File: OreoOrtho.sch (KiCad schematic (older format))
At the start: 44 parts, among them SW1 MXSwitch, SW2 MXSwitch, SW3 MXSwitch, SW4 MXSwitch, SW5 MXSwitch, SW6 MXSwitch, SW7 MXSwitch, SW8 MXSwitch, U1 ATmega32U4-AU, Y1 16MHz

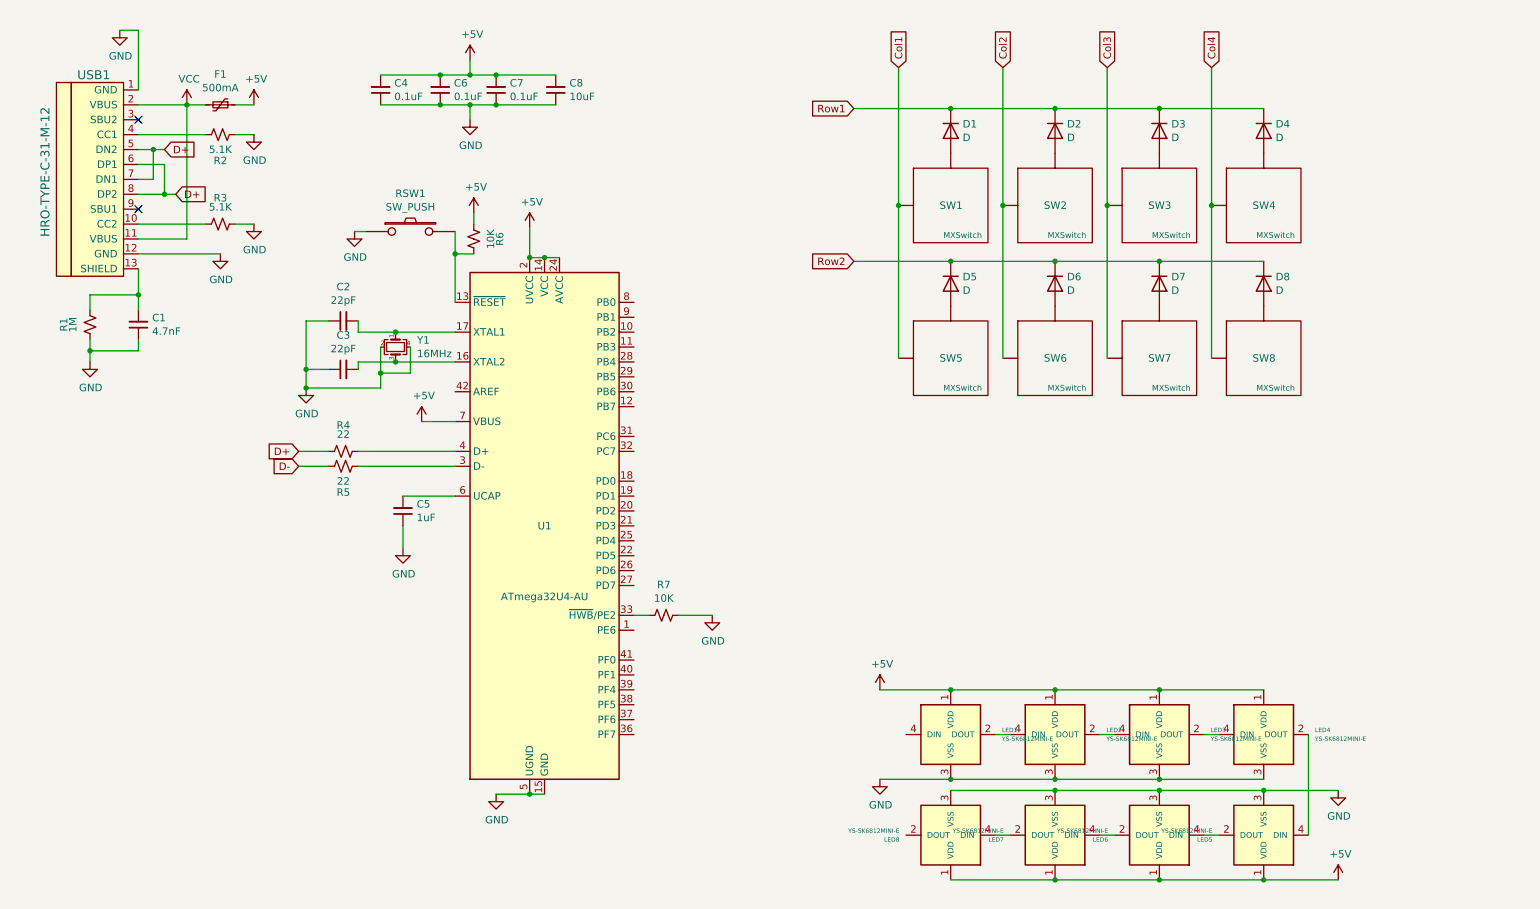
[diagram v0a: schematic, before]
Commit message: new mcu, fuse, etc
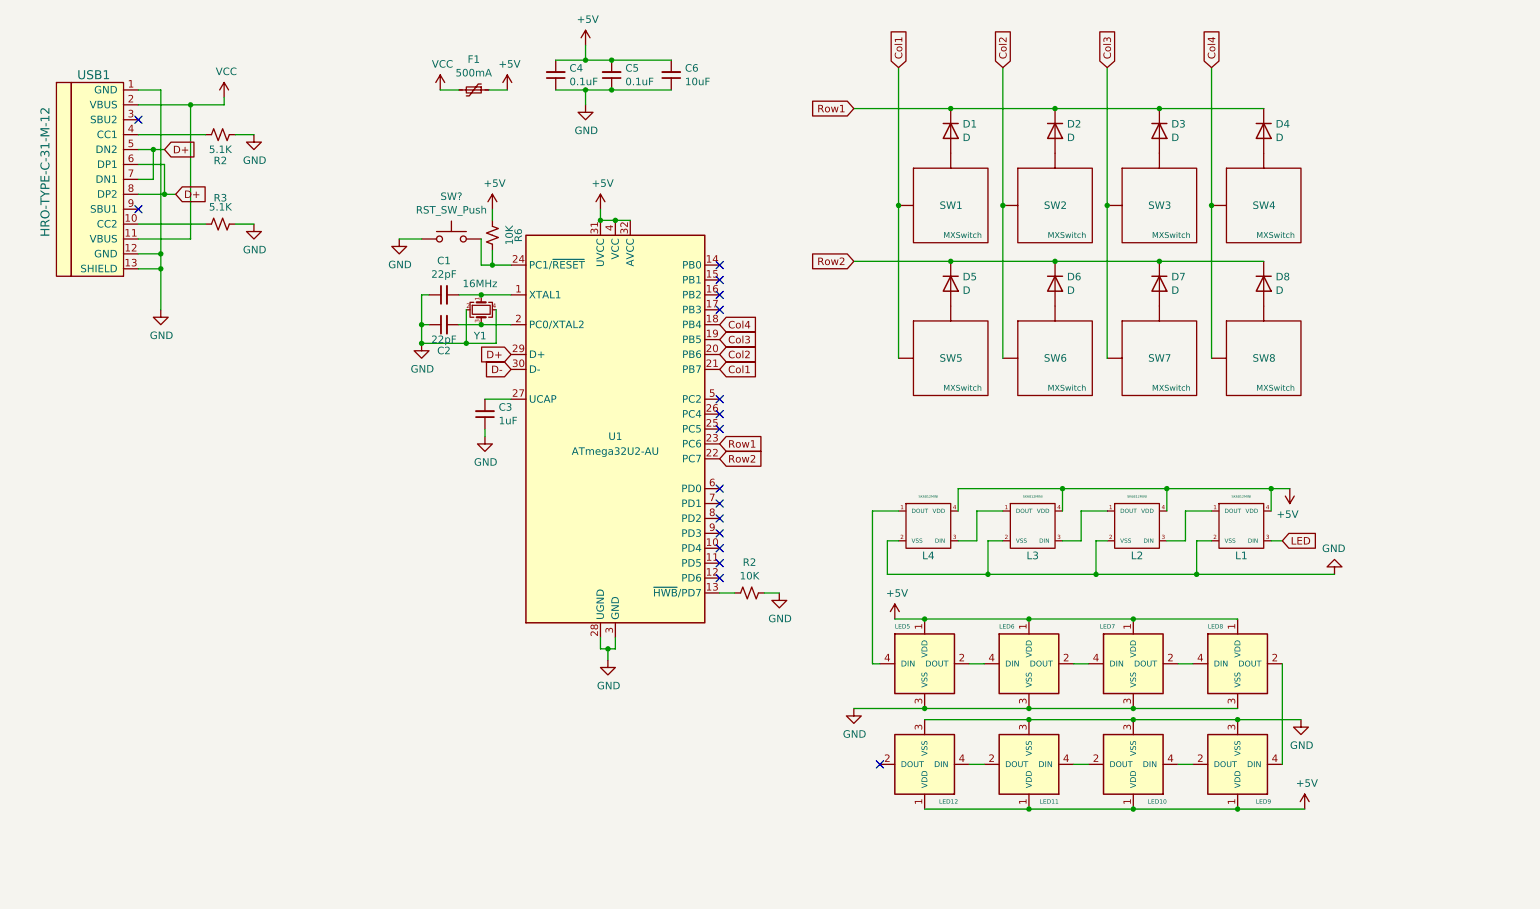
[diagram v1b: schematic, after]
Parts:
- removed C1: 4.7nF, symbol Device:C_Small
- removed C4: 0.1uF, symbol Device:C_Small
- removed R1: 1M, symbol Device:R_Small_US
- removed R4, R5: 22, symbol Device:R_Small_US
- removed RSW1: SW_PUSH, symbol kbd:SW_PUSH
- removed U1: ATmega32U4-AU, Package_QFP:TQFP-44_10x10mm_P0.8mm, symbol MCU_Microchip_ATmega:ATmega32U4-AU
- added L1, L2, L3, L4: SK6812MINI, LED_SMD:LED_SK6812MINI_PLCC4_3.5x3.5mm_P1.75mm, symbol kbd:SK6812MINI
- added SW?: RST_SW_Push, symbol Switch:SW_Push
- added U1: ATmega32U2-AU, Package_QFP:TQFP-32_7x7mm_P0.8mm, symbol MCU_Microchip_ATmega:ATmega32U2-AU
- C1: renamed from C3; footprint (none) -> Capacitor_SMD:C_0805_2012Metric
- C2: footprint (none) -> Capacitor_SMD:C_0805_2012Metric
- C3: renamed from C5; footprint (none) -> Capacitor_SMD:C_0805_2012Metric
- C4: renamed from C6; footprint (none) -> Capacitor_SMD:C_0805_2012Metric
- C5: renamed from C7; footprint (none) -> Capacitor_SMD:C_0805_2012Metric
- C6: renamed from C8; footprint (none) -> Capacitor_SMD:C_0805_2012Metric
- D1, D2, D3, D4, D5, D6, D7, D8: footprint (none) -> Diode_SMD:D_SOD-123
- F1: footprint (none) -> Fuse:Fuse_1206_3216Metric
- LED10: renamed from LED4; footprint (none) -> kbd:SK6812-MINI-E
- LED11: renamed from LED3; footprint (none) -> kbd:SK6812-MINI-E
- LED12: renamed from LED8; footprint (none) -> kbd:SK6812-MINI-E
- LED5, LED6: footprint (none) -> kbd:SK6812-MINI-E
- LED7: renamed from LED2; footprint (none) -> kbd:SK6812-MINI-E
- LED8: renamed from LED7; footprint (none) -> kbd:SK6812-MINI-E
- LED9: renamed from LED1; footprint (none) -> kbd:SK6812-MINI-E
- R2: renamed from R7; footprint (none) -> Resistor_SMD:R_0805_2012Metric
- R2, R3, R6: footprint (none) -> Resistor_SMD:R_0805_2012Metric
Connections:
- net +5V: now also L1.4 (VDD), L2.4 (VDD), L3.4 (VDD), L4.4 (VDD), U1.31 (UVCC), U1.32 (AVCC), U1.4 (VCC)
- net Col1: now also U1.21 (PB7)
- net Col2: now also U1.20 (PB6)
- net Col3: now also U1.19 (PB5)
- net Col4: now also U1.18 (PB4)
- net D+: now also U1.29 (D+)
- net D-: now also U1.30 (D-)
- net GND: now also USB1.13 (SHIELD), L1.2 (VSS), L2.2 (VSS), L3.2 (VSS), L4.2 (VSS), SW?.1, U1.28 (UGND), U1.3 (GND)
- net Row1: now also U1.23 (PC6)
- net Row2: now also U1.22 (PC7)
- net at R6.1: now also SW?.2, U1.24 (PC1/~RESET)
- net at C1.2: now also Y1.1, U1.1 (XTAL1); no longer Y1.3
- net at C2.2: now also Y1.3, U1.2 (PC0/XTAL2); no longer Y1.1
- net at R2.2: now also U1.13 (~HWB~/PD7)
- net at C3.2: now also U1.27 (UCAP)
- net at LED7.2 (DOUT): now also LED8.4 (DIN); no longer LED11.4 (DIN)
- net at LED7.4 (DIN): now also LED6.2 (DOUT); no longer LED9.2 (DOUT)
- net at LED11.2 (DOUT): now also LED12.4 (DIN); no longer LED10.4 (DIN)
- net at LED10.2 (DOUT): now also LED11.4 (DIN); no longer LED5.4 (DIN)
- net at LED8.2 (DOUT): now also LED9.4 (DIN); no longer LED12.4 (DIN)
- new net: LED10.4 (DIN), LED9.2 (DOUT)
- new net: L4.1 (DOUT), LED5.4 (DIN)
- new net: L1.1 (DOUT), L2.3 (DIN)
- new net: L2.1 (DOUT), L3.3 (DIN)
- new net: L3.1 (DOUT), L4.3 (DIN)
- new net LED: L1.3 (DIN)
- no-connect marks 2 -> 17
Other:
- moved on the sheet: C1, C2, C3, C4, C5, C6, F1, LED10, LED11, LED12, LED5, LED6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

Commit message: changed mcu, usb
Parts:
- removed D7, D8: D, Diode_SMD:D_SOD-123, symbol Device:D
- removed L1, L2, L3, L4: SK6812MINI, LED_SMD:LED_SK6812MINI_PLCC4_3.5x3.5mm_P1.75mm, symbol kbd:SK6812MINI
- removed LED8, LED9: YS-SK6812MINI-E, kbd:SK6812-MINI-E, symbol kbd:YS-SK6812MINI-E
- removed SW2, SW3, SW4, SW5, SW6, SW7, SW8: MXSwitch, symbol acheronSymbols:MXSwitch
- added R4, R5: 22, Resistor_SMD:R_0805_2012Metric, symbol Device:R_Small_US
- added SW2, SW3, SW4, SW5, SW6: MXSwitch, kbd:CherryMX_1u, symbol kbd:SW_PUSH
- added U2: PRTR5V0U2X, Package_TO_SOT_SMD:SOT-143, symbol Power_Protection:PRTR5V0U2X
- C1, C2, C3, C4, C5, C6: footprint Capacitor_SMD:C_0805_2012Metric -> Capacitor_SMD:C_0603_1608Metric
- D1, D2, D3, D4, D5, D6: footprint Diode_SMD:D_SOD-123 -> kbd:D3_SMD_v2
- LED1: renamed from LED5; footprint kbd:SK6812-MINI-E -> kbd:YS-SK6812MINI-E
- LED2: renamed from LED6; footprint kbd:SK6812-MINI-E -> kbd:YS-SK6812MINI-E
- LED3: renamed from LED7; footprint kbd:SK6812-MINI-E -> kbd:YS-SK6812MINI-E
- LED4: renamed from LED10; footprint kbd:SK6812-MINI-E -> kbd:YS-SK6812MINI-E
- LED5: renamed from LED11; footprint kbd:SK6812-MINI-E -> kbd:YS-SK6812MINI-E
- LED6: renamed from LED12; footprint kbd:SK6812-MINI-E -> kbd:YS-SK6812MINI-E
- RST_SW1: renamed from SW?; value RST_SW_Push -> SW_Push; footprint (none) -> random-keyboard-parts:SKQG-1155865
- SW1: footprint (none) -> kbd:CherryMX_1u; symbol acheronSymbols:MXSwitch -> kbd:SW_PUSH
- USB1: footprint (none) -> Type-C:HRO-TYPE-C-31-M-12-Assembly; symbol keebio:HRO-TYPE-C-31-M-12 -> Type-C:HRO-TYPE-C-31-M-12
- Y1: footprint (none) -> Crystal:Crystal_SMD_3225-4Pin_3.2x2.5mm_HandSoldering
- renumbered R6 to R1, R2 to R3, R3 to R6
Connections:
- net Col3 is gone; now on net Col2: U1.19 (PB5)
- net Col4 is gone; now on net LED: U1.18 (PB4)
- net Col1: now also U1.20 (PB6), SW2.1, SW5.1; no longer SW1.1 (Col), U1.21 (PB7)
- net Col2: now also SW3.1, SW6.1; no longer U1.20 (PB6)
- net D+: now also R4.2; no longer USB1.5 (DN2), USB1.6 (DP1), USB1.7 (DN1), USB1.8 (DP2)
- net D-: now also R5.1
- net GND: now also R3.2, R6.2, U2.1 (GND); no longer R3.1, R6.1
- net LED: now also LED1.4 (DIN)
- net Row1: now also D5.1 (K), D6.1 (K), U1.26 (PC4); no longer D1.1 (K), D2.1 (K), D3.1 (K), U1.23 (PC6)
- net VCC: now also U2.4 (VCC)
- net at D2.2 (A): now also SW2.2
- net at D3.2 (A): now also SW3.2
- net at D4.2 (A): now also SW4.2
- net at USB1.10 (CC2): now also R6.1; no longer R6.2
- net at USB1.4 (CC1): now also R3.1; no longer R3.2
- net at D5.2 (A): now also SW5.2
- net at D6.2 (A): now also SW6.2
- net at LED3.2 (DOUT): now also LED4.4 (DIN)
- net Row0: now reaches U1.5 (PC2)
- net Row0: now also D1.1 (K), D2.1 (K), D3.1 (K)
- removed net Row2: D5.1 (K), D6.1 (K), U1.22 (PC7)
- new net: R5.2, U2.2 (I/O1), USB1.5 (DN2), USB1.7 (DN1)
- new net: R4.1, U2.3 (I/O2), USB1.6 (DP1), USB1.8 (DP2)
- new net Col0: SW1.1, SW4.1, U1.21 (PB7)
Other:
- moved on the sheet: C1, C2, C3, C4, C5, C6, D1, F1, LED1, LED2, LED3, LED4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

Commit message: route ver1
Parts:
- removed D3, D6: D, kbd:D3_SMD_v2, symbol Device:D
- removed LED5, LED6: YS-SK6812MINI-E, kbd:YS-SK6812MINI-E, symbol kbd:YS-SK6812MINI-E
- removed SW3, SW6: MXSwitch, kbd:CherryMX_1u, symbol kbd:SW_PUSH
- added H1: MountingHole, kbd:HOLE, symbol Mechanical:MountingHole
- renumbered D4 to D3, D5 to D4, SW4 to SW3, SW5 to SW4
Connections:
- net Row0: now also U1.23 (PC6); no longer U1.5 (PC2)
- net Row1: now also U1.22 (PC7); no longer U1.26 (PC4)
- net Col2: no longer names the net of U1.19 (PB5)
- no-connect marks 17 -> 18
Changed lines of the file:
@@
 Wire Wire Line
 	1925 4250 1925 4450
-Text GLabel 5825 2425 2    50   Input ~ 0
+Text GLabel 5825 2725 2    50   Input ~ 0
 Row1
 Text GLabel 5825 2025 2    50   Input ~ 0
 Col1
-Text GLabel 5825 1925 2    50   Input ~ 0
-Col2
 $Comp
 L MCU_Microchip_ATmega:ATmega32U2-AU U1
@@
 Wire Wire Line
 	8025 1375 8025 1950
-Connection ~ 8725 1375
-Wire Wire Line
-	8725 1375 8725 1950
-Connection ~ 9425 1375
-Wire Wire Line
-	9425 1375 9425 1950
-Connection ~ 9325 1675
-Connection ~ 9325 2250
-$Comp
-L kbd:SW_PUSH SW4
+$Comp
+L kbd:SW_PUSH SW3
 U 1 1 60136BE3
 P 8325 1950
-F 0 "SW4" H 8250 1950 50  0000 L CNN
+F 0 "SW3" H 8250 1950 50  0000 L CNN
 F 1 "MXSwitch" H 8175 1875 39  0000 L CNN
 F 2 "kbd:CherryMX_1u" H 8325 1950 50  0001 C CNN
@@
 	8475 2250 8625 2250
 $Comp
-L kbd:SW_PUSH SW5
+L kbd:SW_PUSH SW4
 U 1 1 60136BF5
 P 9025 1950
-F 0 "SW5" H 8950 1950 50  0000 L CNN
+F 0 "SW4" H 8950 1950 50  0000 L CNN
 F 1 "MXSwitch" H 8875 1875 39  0000 L CNN
 F 2 "kbd:CherryMX_1u" H 9025 1950 50  0001 C CNN
@@
 $EndComp
 $Comp
-L Device:D D5
+L Device:D D4
 U 1 1 60136BFB
 P 9325 2100
-F 0 "D5" H 9275 2225 50  0000 L CNN
+F 0 "D4" H 9275 2225 50  0000 L CNN
 F 1 "D" H 9300 2000 50  0000 L CNN
 F 2 "kbd:D3_SMD_v2" H 9325 2100 50  0001 C CNN
@@
 $EndComp
 Connection ~ 8625 2250
-$Comp
-L kbd:SW_PUSH SW6
-U 1 1 60136C05
-P 9725 1950
-F 0 "SW6" H 9650 1950 50  0000 L CNN
-F 1 "MXSwitch" H 9575 1875 39  0000 L CNN
-F 2 "kbd:CherryMX_1u" H 9725 1950 50  0001 C CNN
-F 3 "" H 9725 1950 50  0001 C CNN
-	1    9725 1950
-	1    0    0    -1
-$EndComp
-$Comp
-L Device:D D6
-U 1 1 60136C0B
-P 10025 2100
-F 0 "D6" H 9975 2225 50  0000 L CNN
-F 1 "D" H 10000 2000 50  0000 L CNN
-F 2 "kbd:D3_SMD_v2" H 10025 2100 50  0001 C CNN
-F 3 "~" H 10025 2100 50  0001 C CNN
-	1    10025 2100
-	0    -1   -1   0
-$EndComp
-Wire Wire Line
-	9325 2250 10025 2250
-Wire Wire Line
-	9325 1675 10025 1675
-Wire Wire Line
-	9425 1375 9425 1150
-$Comp
-L Device:D D3
-U 1 1 6012380C
-P 10025 1525
-F 0 "D3" H 9975 1650 50  0000 L CNN
-F 1 "D" H 10000 1425 50  0000 L CNN
-F 2 "kbd:D3_SMD_v2" H 10025 1525 50  0001 C CNN
-F 3 "~" H 10025 1525 50  0001 C CNN
-	1    10025 1525
-	0    -1   -1   0
-$EndComp
-$Comp
-L kbd:SW_PUSH SW3
-U 1 1 60123806
-P 9725 1375
-F 0 "SW3" H 9650 1375 50  0000 L CNN
-F 1 "MXSwitch" H 9575 1300 39  0000 L CNN
-F 2 "kbd:CherryMX_1u" H 9725 1375 50  0001 C CNN
-F 3 "" H 9725 1375 50  0001 C CNN
-	1    9725 1375
-	1    0    0    -1
-$EndComp
-Text GLabel 9425 1150 1    50   Input ~ 0
-Col2
 Connection ~ 8625 1675
 Wire Wire Line
 	8625 1675 9325 1675
-Wire Wire Line
-	8725 1375 8725 1150
 $Comp
 L Device:D D2
@@
 	0    -1   -1   0
 $EndComp
-$Comp
-L kbd:SW_PUSH SW2
-U 1 1 6011665D
-P 9025 1375
-F 0 "SW2" H 8950 1375 50  0000 L CNN
-F 1 "MXSwitch" H 8875 1300 39  0000 L CNN
-F 2 "kbd:CherryMX_1u" H 9025 1375 50  0001 C CNN
-F 3 "" H 9025 1375 50  0001 C CNN
-	1    9025 1375
-	1    0    0    -1
-$EndComp
 Wire Wire Line
 	8025 1375 8025 1150
@@
 Wire Wire Line
 	7575 4000 7625 4000
-NoConn ~ 7625 4675
+NoConn ~ 9025 4675
 Text GLabel 7575 4000 0    50   Input ~ 0
 LED
@@
 $EndComp
 Wire Wire Line
-	8625 4975 9325 4975
-Connection ~ 8625 4975
-Connection ~ 8625 4375
-Wire Wire Line
-	7925 4375 8625 4375
-Wire Wire Line
-	7925 4975 8625 4975
-Wire Wire Line
 	8225 4000 8325 4000
 $Comp
@@
 	9725 4000 9725 4675
 Wire Wire Line
-	8325 4675 8225 4675
-Wire Wire Line
-	9025 4675 8925 4675
-Wire Wire Line
 	9725 4675 9625 4675
-$Comp
-L kbd:YS-SK6812MINI-E LED6
-U 1 1 5F923BDB
-P 7925 4675
-F 0 "LED6" H 7700 4925 29  0000 L CNN
-F 1 "YS-SK6812MINI-E" H 8269 4646 29  0001 L CNN
-F 2 "kbd:YS-SK6812MINI-E" H 8025 4425 50  0001 C CNN
-F 3 "" H 8025 4425 50  0001 C CNN
-	1    7925 4675
-	-1   0    0    1
-$EndComp
 $Comp
 L kbd:YS-SK6812MINI-E LED2
@@
 	8925 4000 9025 4000
 $Comp
-L kbd:YS-SK6812MINI-E LED5
-U 1 1 5F8F9075
-P 8625 4675
-F 0 "LED5" H 8425 4925 29  0000 L CNN
-F 1 "YS-SK6812MINI-E" H 8969 4646 29  0001 L CNN
-F 2 "kbd:YS-SK6812MINI-E" H 8725 4425 50  0001 C CNN
-F 3 "" H 8725 4425 50  0001 C CNN
-	1    8625 4675
-	-1   0    0    1
-$EndComp
-$Comp
 L kbd:YS-SK6812MINI-E LED3
 U 1 1 5F8F886B
@@
 Text GLabel 5825 2125 2    50   Input ~ 0
 Col0
-Text GLabel 5825 2325 2    50   Input ~ 0
+Text GLabel 5825 2625 2    50   Input ~ 0
 Row0
 NoConn ~ 5825 1725
 Text GLabel 5825 1825 2    50   Input ~ 0
 LED
-Wire Wire Line
-	8625 4375 9325 4375
-Connection ~ 9325 4375
 $Comp
 L kbd:YS-SK6812MINI-E LED4
@@
 	-1   0    0    1
 $EndComp
-Connection ~ 9325 4975
 Wire Wire Line
 	1325 1500 1700 1500
@@
 Connection ~ 1775 3850
 NoConn ~ 5825 2525
-NoConn ~ 5825 2625
-NoConn ~ 5825 2725
+NoConn ~ 5825 2425
+NoConn ~ 5825 2325
 Wire Wire Line
 	9325 4975 9775 4975
@@
 	9325 4375 9900 4375
 $Comp
-L Device:D D4
+L Device:D D3
 U 1 1 60136BE9
 P 8625 2100
-F 0 "D4" H 8575 2225 50  0000 L CNN
+F 0 "D3" H 8575 2225 50  0000 L CNN
 F 1 "D" H 8600 2000 50  0000 L CNN
 F 2 "kbd:D3_SMD_v2" H 8625 2100 50  0001 C CNN
@@
 	0    -1   -1   0
 $EndComp
+Wire Wire Line
+	8725 1375 8725 1150
+Wire Wire Line
+	8725 1375 8725 1950
+Connection ~ 8725 1375
+$Comp
+L kbd:SW_PUSH SW2
+U 1 1 6011665D
+P 9025 1375
+F 0 "SW2" H 8950 1375 50  0000 L CNN
+F 1 "MXSwitch" H 8875 1300 39  0000 L CNN
+F 2 "kbd:CherryMX_1u" H 9025 1375 50  0001 C CNN
+F 3 "" H 9025 1375 50  0001 C CNN
+	1    9025 1375
+	1    0    0    -1
+$EndComp
+NoConn ~ 5825 1925
+$Comp
+L Mechanical:MountingHole H1
+U 1 1 5F929254
+P 1025 5700
+F 0 "H1" H 1125 5746 50  0000 L CNN
+F 1 "MountingHole" H 1125 5655 50  0000 L CNN
+F 2 "kbd:HOLE" H 1025 5700 50  0001 C CNN
+F 3 "~" H 1025 5700 50  0001 C CNN
+	1    1025 5700
+	1    0    0    -1
+$EndComp
 $EndSCHEMATC

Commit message: reroute
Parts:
- SW1, SW2, SW3, SW4: footprint kbd:CherryMX_1u -> kbd:CherryMX_Hotswap
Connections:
- net Col0: now also U1.10 (PD4); no longer U1.21 (PB7)
- net Col1: now also U1.9 (PD3); no longer U1.20 (PB6)
- net LED: now also U1.8 (PD2); no longer U1.18 (PB4)
- net Row0: now also U1.15 (PB1); no longer U1.23 (PC6)
- net Row1: now also U1.16 (PB2); no longer U1.22 (PC7)
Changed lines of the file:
@@
 Wire Wire Line
 	1925 4250 1925 4450
-Text GLabel 5825 2725 2    50   Input ~ 0
+Text GLabel 5825 1625 2    50   Input ~ 0
 Row1
-Text GLabel 5825 2025 2    50   Input ~ 0
+Text GLabel 5825 3225 2    50   Input ~ 0
 Col1
 $Comp
@@
 $EndComp
 NoConn ~ 5825 1425
-NoConn ~ 5825 1525
-NoConn ~ 5825 1625
+NoConn ~ 5825 2725
+NoConn ~ 5825 2625
 NoConn ~ 5825 2925
 NoConn ~ 5825 3025
-NoConn ~ 5825 3125
-NoConn ~ 5825 3225
-NoConn ~ 5825 3325
+NoConn ~ 5825 2025
+NoConn ~ 5825 1825
+NoConn ~ 5825 2125
 NoConn ~ 5825 3425
 NoConn ~ 5825 3525
@@
 F 0 "SW3" H 8250 1950 50  0000 L CNN
 F 1 "MXSwitch" H 8175 1875 39  0000 L CNN
-F 2 "kbd:CherryMX_1u" H 8325 1950 50  0001 C CNN
+F 2 "kbd:CherryMX_Hotswap" H 8325 1950 50  0001 C CNN
 F 3 "" H 8325 1950 50  0001 C CNN
 	1    8325 1950
@@
 F 0 "SW4" H 8950 1950 50  0000 L CNN
 F 1 "MXSwitch" H 8875 1875 39  0000 L CNN
-F 2 "kbd:CherryMX_1u" H 9025 1950 50  0001 C CNN
+F 2 "kbd:CherryMX_Hotswap" H 9025 1950 50  0001 C CNN
 F 3 "" H 9025 1950 50  0001 C CNN
 	1    9025 1950
@@
 F 0 "SW1" H 8250 1375 50  0000 L CNN
 F 1 "MXSwitch" H 8175 1300 39  0000 L CNN
-F 2 "kbd:CherryMX_1u" H 8325 1375 50  0001 C CNN
+F 2 "kbd:CherryMX_Hotswap" H 8325 1375 50  0001 C CNN
 F 3 "" H 8325 1375 50  0001 C CNN
 	1    8325 1375
@@
 	1    0    0    -1
 $EndComp
-Text GLabel 5825 2125 2    50   Input ~ 0
+Text GLabel 5825 3325 2    50   Input ~ 0
 Col0
-Text GLabel 5825 2625 2    50   Input ~ 0
+Text GLabel 5825 1525 2    50   Input ~ 0
 Row0
 NoConn ~ 5825 1725
-Text GLabel 5825 1825 2    50   Input ~ 0
+Text GLabel 5825 3125 2    50   Input ~ 0
 LED
 $Comp
@@
 F 0 "SW2" H 8950 1375 50  0000 L CNN
 F 1 "MXSwitch" H 8875 1300 39  0000 L CNN
-F 2 "kbd:CherryMX_1u" H 9025 1375 50  0001 C CNN
+F 2 "kbd:CherryMX_Hotswap" H 9025 1375 50  0001 C CNN
 F 3 "" H 9025 1375 50  0001 C CNN
 	1    9025 1375

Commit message: minor file changes
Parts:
- added C7: 0.1uF, Capacitor_SMD:C_0603_1608Metric, symbol Device:C_Small
- added G2: Oreo, doggy:bike, symbol oreo:LOGO
- SW1, SW2, SW3, SW4: footprint kbd:CherryMX_Hotswap -> doggy:CherryMX_Hotswap_clear
- U1: value ATmega32U2-AU -> ATmega32U4-AU; footprint Package_QFP:TQFP-32_7x7mm_P0.8mm -> Package_QFP:TQFP-44_10x10mm_P0.8mm; symbol MCU_Microchip_ATmega:ATmega32U2-AU -> MCU_Microchip_ATmega:ATmega32U4-AU
- USB1: footprint Type-C:HRO-TYPE-C-31-M-12-Assembly -> Type-C:HRO-TYPE-C-31-M-12
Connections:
- net +5V: now also U1.14 (VCC), U1.2 (UVCC), U1.24 (AVCC), U1.34 (VCC), U1.44 (AVCC), U1.7 (VBUS), C7.2; no longer U1.31 (UVCC), U1.32 (AVCC), U1.4 (VCC)
- net Col0: now also U1.12 (PB7); no longer U1.10 (PD4)
- net Col1: now also U1.11 (PB3); no longer U1.9 (PD3)
- net D+: now also U1.4 (D+); no longer U1.29 (D+)
- net D-: now also U1.3 (D-); no longer U1.30 (D-)
- net GND: now also U1.15 (GND), U1.23 (GND), U1.35 (GND), U1.43 (GND), U1.5 (UGND), C7.1; no longer U1.28 (UGND), U1.3 (GND)
- net Row0: now also U1.29 (PB5); no longer U1.15 (PB1)
- net Row1: now also U1.30 (PB6); no longer U1.16 (PB2)
- net at C3.2: now also U1.6 (UCAP); no longer U1.27 (UCAP)
- net at R2.2: now also U1.33 (~HWB~/PE2); no longer U1.13 (~HWB~/PD7)
- net at C1.2, Y1.1: now also U1.17 (XTAL1); no longer U1.1 (XTAL1)
- net at C2.2, Y1.3: now also U1.16 (XTAL2); no longer U1.2 (PC0/XTAL2)
- net RST: now reaches R1.1, RST_SW1.2
- net RST: now also U1.13 (~RESET); no longer U1.24 (PC1/~RESET)
- no-connect marks 18 -> 24
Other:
- moved on the sheet: C1, C2, C3, C4, C5, C6, D1, D2, D3, D4, F1, H1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
